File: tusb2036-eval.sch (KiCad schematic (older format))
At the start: 54 parts, among them J1 USB_B_Micro, J2 USB_A, J3 USB_A, J4 USB_A, SW1 RESET, U1 TUSB2036, U2 TPS76333, U3 TPS2044D, U4 SN75240, U5 SN75240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

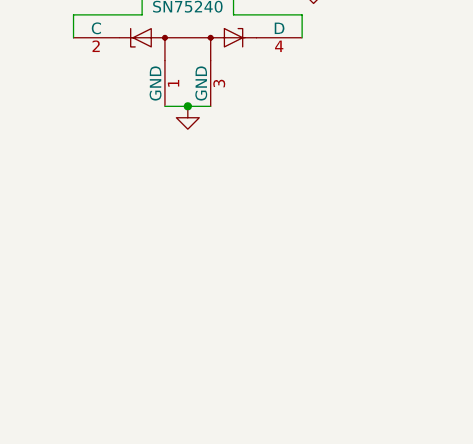
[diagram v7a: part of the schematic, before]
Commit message: Add OSHW logo
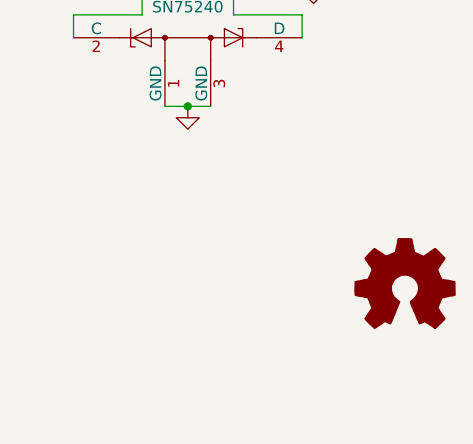
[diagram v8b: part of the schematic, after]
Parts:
- added LOGO1: Logo_Open_Hardware_Small, Symbol:OSHW-Logo2_9.8x8mm_SilkScreen, symbol Graphic:Logo_Open_Hardware_Small
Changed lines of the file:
@@
 Wire Wire Line
 	9350 2850 9350 3050
+$Comp
+L Graphic:Logo_Open_Hardware_Small LOGO1
+U 1 1 6088030F
+P 10200 7100
+F 0 "LOGO1" H 10200 7375 50  0001 C CNN
+F 1 "Logo_Open_Hardware_Small" H 10200 6875 50  0001 C CNN
+F 2 "Symbol:OSHW-Logo2_9.8x8mm_SilkScreen" H 10200 7100 50  0001 C CNN
+F 3 "~" H 10200 7100 50  0001 C CNN
+	1    10200 7100
+	1    0    0    -1
+$EndComp
 $EndSCHEMATC
